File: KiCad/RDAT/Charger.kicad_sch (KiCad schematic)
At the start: 52 parts, among them U6 BQ24617RGER

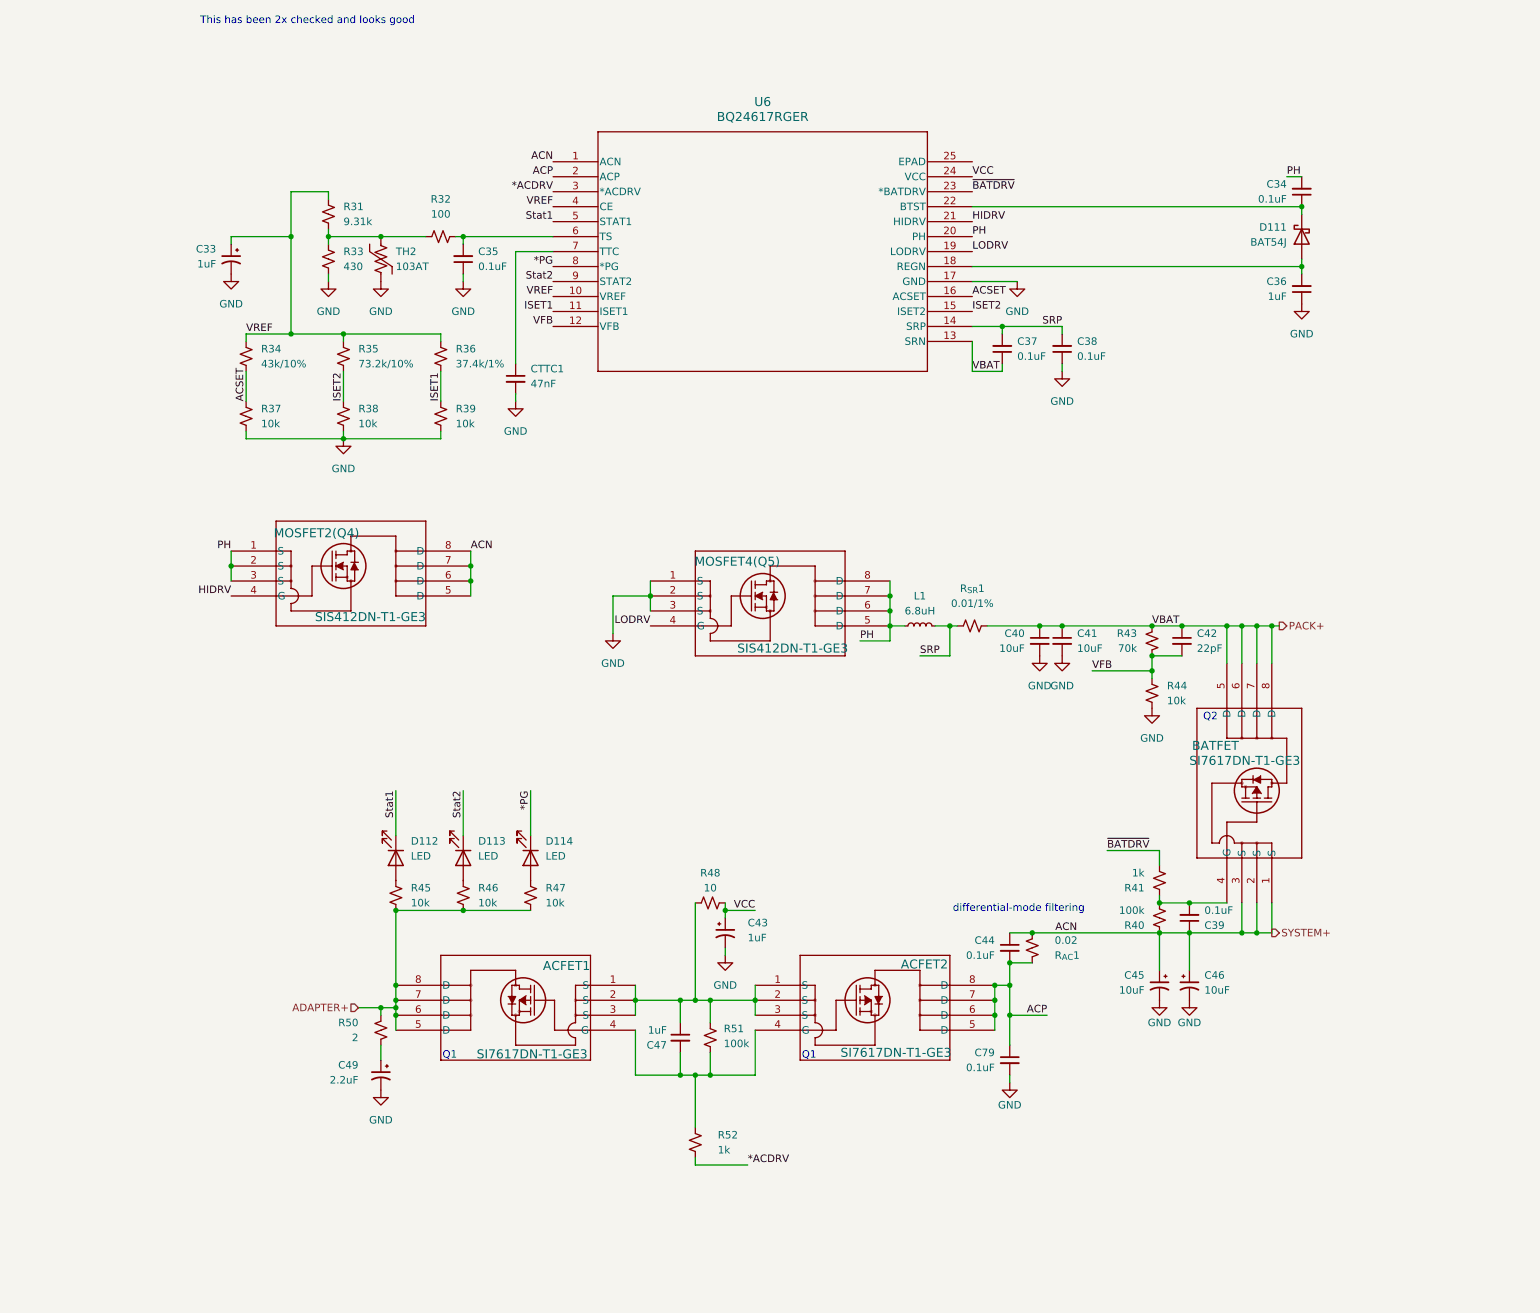
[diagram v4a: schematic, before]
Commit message: Added Libs and DOCS
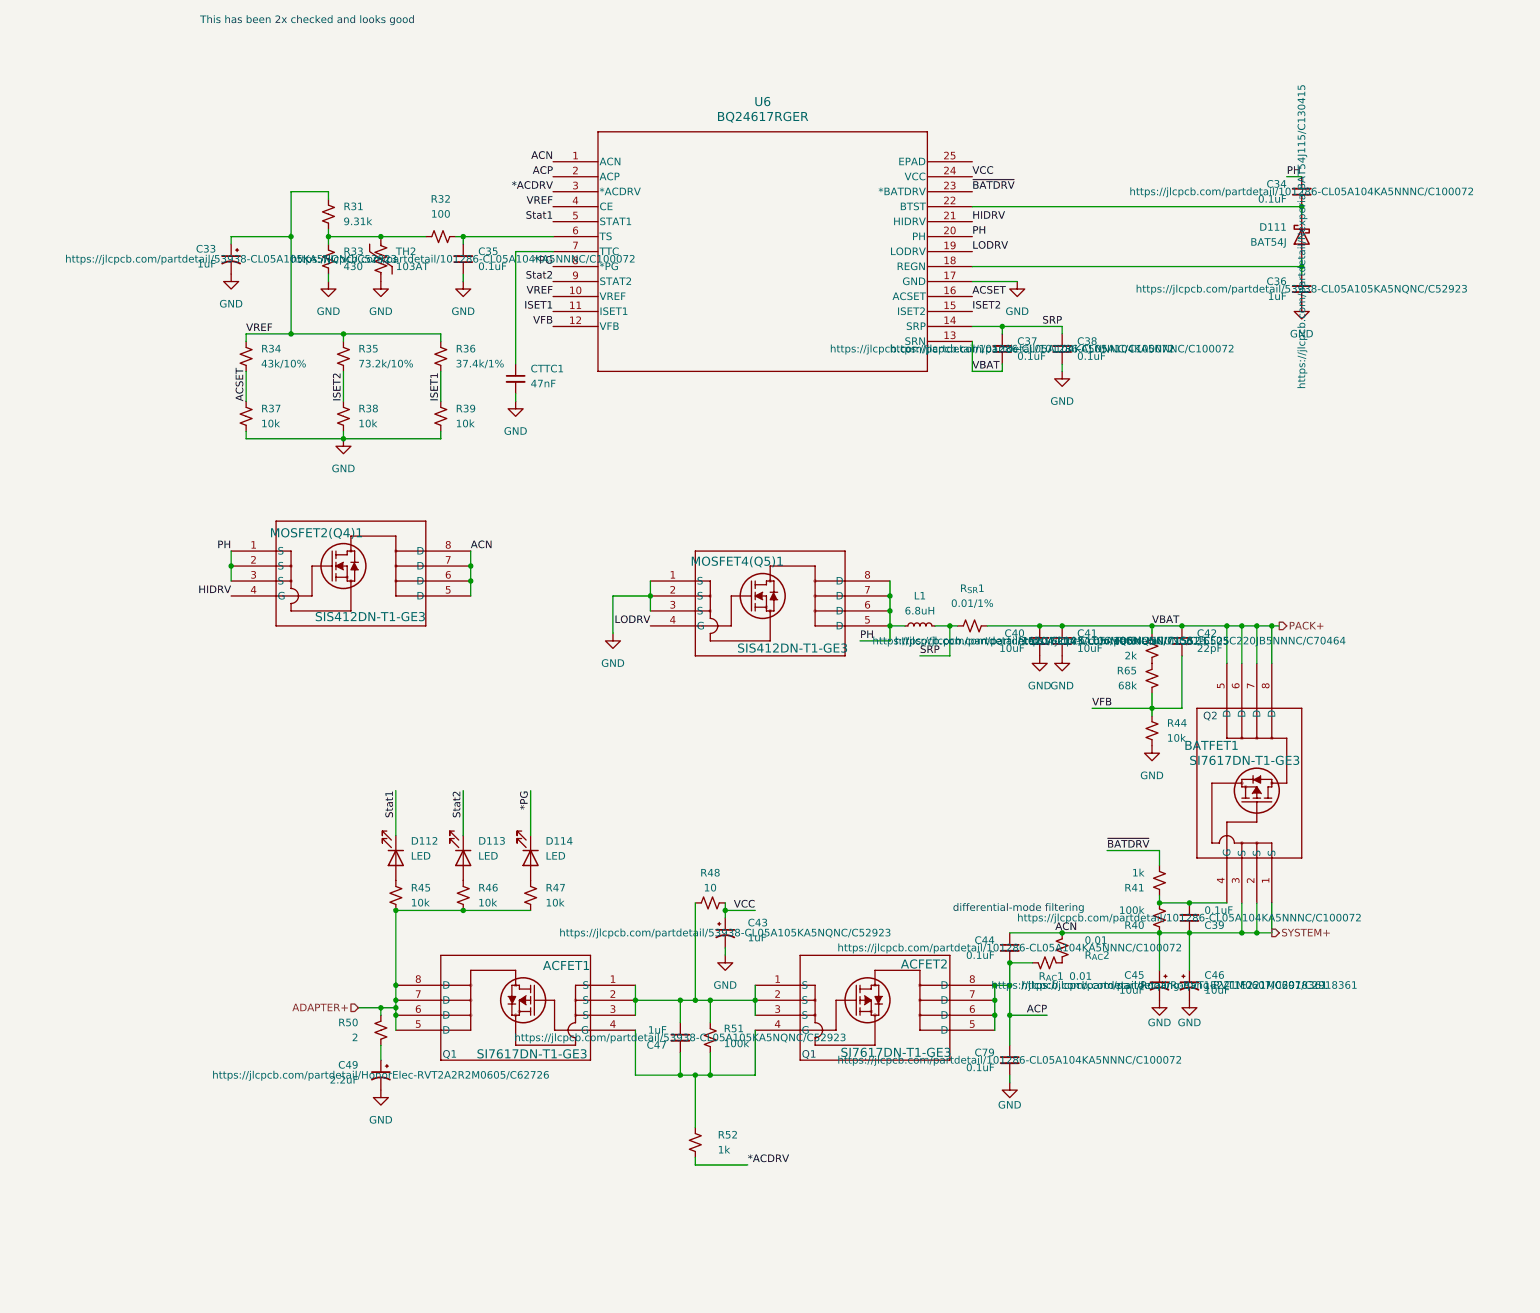
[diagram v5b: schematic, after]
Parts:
- added R65: 68k, Resistor_SMD:R_0402_1005Metric, symbol Device:R_Small_US
- added R_{AC}2: 0.01, footprints:RESC_WSHM2818R0150FEA, symbol Device:R_Small_US
- C33, C36, C43, C47: JLCPCB_LINK (none) -> https://jlcpcb.com/partdetail/53938-CL05A105KA5NQNC/C52923
- C34, C35, C37, C38, C39, C44, C79: JLCPCB_LINK (none) -> https://jlcpcb.com/partdetail/101286-CL05A104KA5NNNC/C100072
- C40, C41: JLCPCB_LINK (none) -> https://jlcpcb.com/partdetail/16204-CL05A106MQ5NUNC/C15525
- C42: JLCPCB_LINK (none) -> https://jlcpcb.com/partdetail/71561-CL05C220JB5NNNC/C70464
- C45, C46: JLCPCB_LINK (none) -> https://jlcpcb.com/partdetail/Roqang-RVT1E221M0607/C2918361
- C49: JLCPCB_LINK (none) -> https://jlcpcb.com/partdetail/HonorElec-RVT2A2R2M0605/C62726
- CTTC1: JLCPCB_LINK (none) -> https://jlcpcb.com/partdetail/291013-CL05B473KB5VPNC/C307339
- D111: JLCPCB_LINK (none) -> https://jlcpcb.com/partdetail/Nexperia-BAT54J115/C130415
- L1: JLCPCB_LINK (none) -> https://jlcpcb.com/partdetail/VishayIntertech-IHLP2525EZER6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
- MOSFET2(Q4)1: renamed from MOSFET2(Q4); JLCPCB_LINK (none) -> https://jlcpcb.com/partdetail/VishayIntertech-SIS412DN_T1GE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
- MOSFET4(Q5)1: renamed from MOSFET4(Q5); JLCPCB_LINK (none) -> https://jlcpcb.com/partdetail/VishayIntertech-SIS412DN_T1GE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
- R32: footprint (none) -> Resistor_SMD:R_0402_1005Metric; JLCPCB_LINK (none) -> https://jlcpcb.com/partdetail/25819-0402WGF1000TCE/C25076
- R33: JLCPCB_LINK (none) -> https://jlcpcb.com/partdetail/37334-0402WGF4300TCE/C36356
- R34: JLCPCB_LINK (none) -> https://jlcpcb.com/partdetail/Ralec-RTT0243R0FTH/C11563
- R37, R38, R39, R44, R45, R46, R47: footprint (none) -> Resistor_SMD:R_0402_1005Metric; JLCPCB_LINK (none) -> https://jlcpcb.com/partdetail/26487-0402WGF1002TCE/C25744
- R40, R51: footprint (none) -> Resistor_SMD:R_0402_1005Metric; JLCPCB_LINK (none) -> https://jlcpcb.com/partdetail/26484-0402WGF1003TCE/C25741
- R41, R52: footprint (none) -> Resistor_SMD:R_0402_1005Metric; JLCPCB_LINK (none) -> https://jlcpcb.com/partdetail/12256-0402WGF1001TCE/C11702
- R43: value 70k -> 2k; footprint (none) -> Resistor_SMD:R_0402_1005Metric; JLCPCB_LINK (none) -> https://jlcpcb.com/partdetail/4516-0402WGF2001TCE/C4109
- R48: JLCPCB_LINK (none) -> https://jlcpcb.com/partdetail/25820-0402WGF100JTCE/C25077
- R50: footprint (none) -> Resistor_SMD:R_0402_1005Metric; JLCPCB_LINK (none) -> https://jlcpcb.com/partdetail/25900-0402WGJ020JTCE/C25157
- R_{AC}1: value 0.02 -> 0.01; footprint (none) -> footprints:RESC_WSHM2818R0150FEA; JLCPCB_LINK (none) -> https://jlcpcb.com/partdetail/VishayIntertech-WSHP2818R0100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
- R_{SR}1: footprint (none) -> footprints:RESC_WSHM2818R0150FEA; JLCPCB_LINK (none) -> https://jlcpcb.com/partdetail/VishayIntertech-WSHP2818R0100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
- TH2: footprint (none) -> Resistor_SMD:R_0603_1608Metric; JLCPCB_LINK (none) -> https://jlcpcb.com/partdetail/MurataElectronics-NCP18XH103F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
- U6: JLCPCB_LINK (none) -> https://jlcpcb.com/partdetail/TexasInstruments-BQ24617RGER/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
- renumbered BATFET to BATFET1
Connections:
- net SYSTEM+: now also R_{AC}2.2; no longer R_{AC}1.2
- net VFB: now also R65.2; no longer R43.2
- new net: R43.2, R65.1
- new net: R_{AC}1.2, R_{AC}2.1
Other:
- moved on the sheet: R43, R44, R_{AC}1

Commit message: Sourced and documented all parts
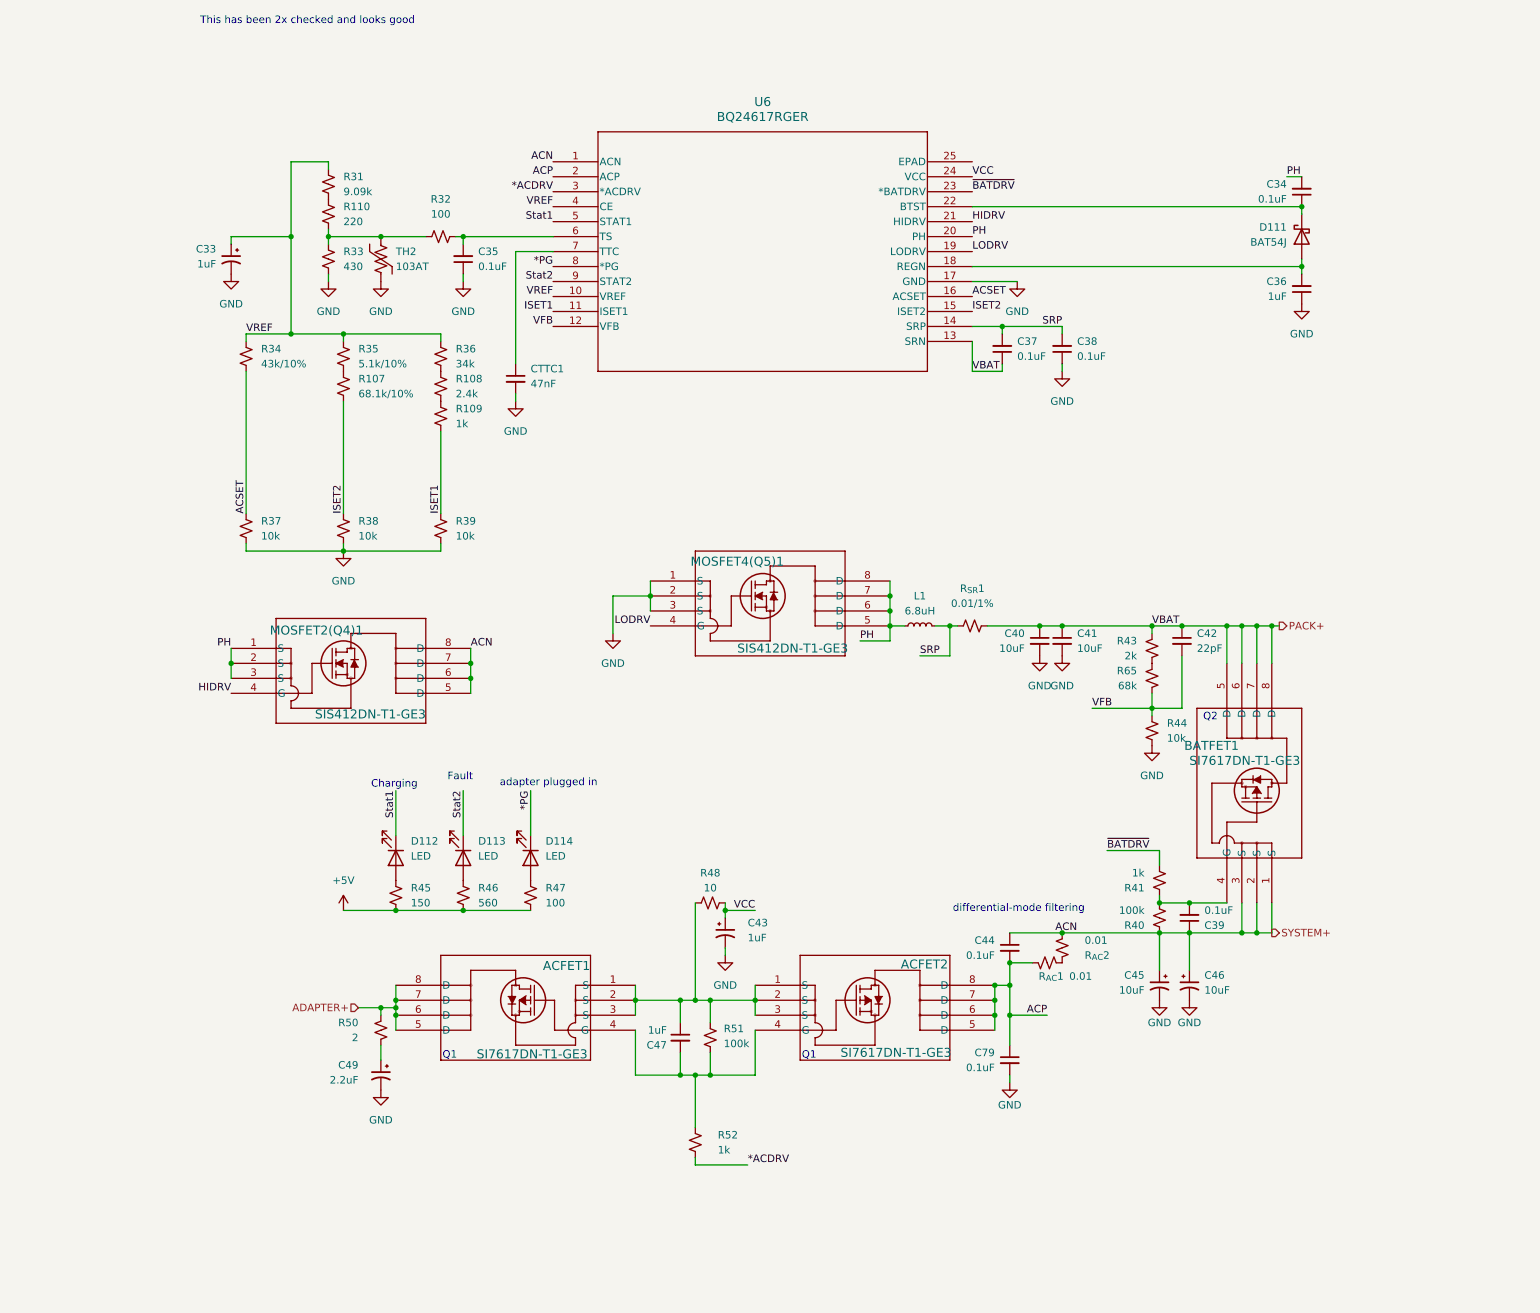
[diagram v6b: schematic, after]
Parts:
- added R107: 68.1k/10%, Resistor_SMD:R_0402_1005Metric, symbol Device:R_Small_US
- added R108: 2.4k, Resistor_SMD:R_0402_1005Metric, symbol Device:R_Small_US
- added R109: 1k, Resistor_SMD:R_0402_1005Metric, symbol Device:R_Small_US
- added R110: 220, Resistor_SMD:R_0402_1005Metric, symbol Device:R_Small_US
- C33, C43: footprint (none) -> footprints:CAP-SMD_BD4.0-L4.3-W4.3-FD; JLCPCB_LINK https://jlcpcb.com/partdetail/53938-CL05A105KA5NQNC/C52923 -> https://jlcpcb.com/partdetail/HonorElec-RVT1H1R0M0405/C3348
- C34, C35, C37, C38, C39, C44, C79: footprint (none) -> Capacitor_SMD:C_0402_1005Metric; JLCPCB_LINK https://jlcpcb.com/partdetail/101286-CL05A104KA5NNNC/C100072 -> https://jlcpcb.com/partdetail/1933-0402F104M500NT/C1581
- C36, C40, C41, C42, C47, CTTC1: footprint (none) -> Capacitor_SMD:C_0402_1005Metric
- C45, C46, C49: footprint (none) -> footprints:CAP-SMD_BD6.3-L6.6-W6.6-LS7.4-FD
- D112: footprint (none) -> Diode_SMD:D_1206_3216Metric; JLCPCB_LINK (none) -> https://jlcpcb.com/partdetail/EverlightElec-11_21_Y2C_CNQBY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
- D113: footprint (none) -> Diode_SMD:D_1206_3216Metric; JLCPCB_LINK (none) -> https://jlcpcb.com/partdetail/Meihua-MHT151CRCT/C559117
- D114: footprint (none) -> Diode_SMD:D_1206_3216Metric; JLCPCB_LINK (none) -> https://jlcpcb.com/partdetail/EverlightElec-15_21_BHC_AP1Q2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
- L1: footprint (none) -> Inductor_SMD:L_Vishay_IHLP-2525; JLCPCB_LINK https://jlcpcb.com/partdetail/VishayIntertech-IHLP2525EZER6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 -> https://jlcpcb.com/partdetail/VishayIntertech-IHLP2525CZER6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
- R31: value 9.31k -> 9.09k; footprint (none) -> Resistor_SMD:R_0402_1005Metric; JLCPCB_LINK (none) -> https://jlcpcb.com/partdetail/12103-0402WGF9091TCE/C11549
- R33, R34, R48: footprint (none) -> Resistor_SMD:R_0402_1005Metric
- R35: value 73.2k/10% -> 5.1k/10%; footprint (none) -> Resistor_SMD:R_0603_1608Metric; JLCPCB_LINK (none) -> https://jlcpcb.com/partdetail/23913-0603WAF5101T5E/C23186
- R36: value 37.4k/1% -> 34k; footprint (none) -> Resistor_SMD:R_0402_1005Metric; JLCPCB_LINK (none) -> https://jlcpcb.com/partdetail/49947-0402WGF3402TCE/C48939
- R45: value 10k -> 150; JLCPCB_LINK https://jlcpcb.com/partdetail/26487-0402WGF1002TCE/C25744 -> https://jlcpcb.com/partdetail/25825-0402WGF1500TCE/C25082
- R46: value 10k -> 560; JLCPCB_LINK https://jlcpcb.com/partdetail/26487-0402WGF1002TCE/C25744 -> https://jlcpcb.com/partdetail/25869-0402WGF5600TCE/C25126
- R47: value 10k -> 100; JLCPCB_LINK https://jlcpcb.com/partdetail/26487-0402WGF1002TCE/C25744 -> https://jlcpcb.com/partdetail/25819-0402WGF1000TCE/C25076
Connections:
- net ADAPTER+: no longer R45.2, R46.2, R47.2
- net ISET1: now also R109.2; no longer R36.2
- net ISET2: now also R107.2; no longer R35.2
- net at R32.1, R33.1, TH2.1: now also R110.2; no longer R31.2
- new net: R107.1, R35.2
- new net: R108.1, R36.2
- new net: R108.2, R109.1
- new net: R110.1, R31.2
- new net +5V: R45.2, R46.2, R47.2
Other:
- note added: "Charging"
- note added: "Fault"
- note added: "adapter plugged in"
- moved on the sheet: MOSFET2(Q4)1, R31, R37, R38, R39
